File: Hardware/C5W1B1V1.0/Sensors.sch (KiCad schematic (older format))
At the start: 23 parts, among them U5 LSM303AHTR, U6 VL53L0CXV0DH_1, U7 BME688, U8 ISM330ISN

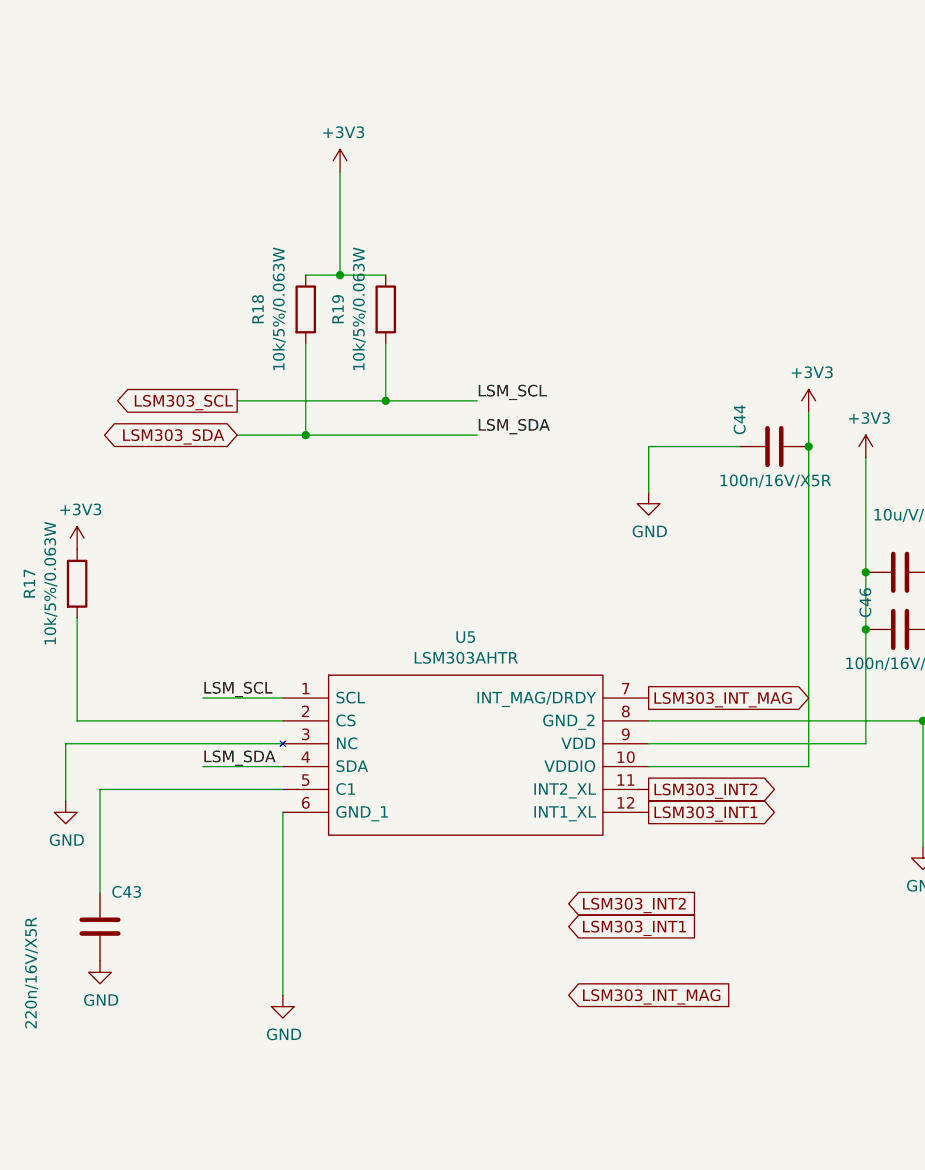
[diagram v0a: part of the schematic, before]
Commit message: Linie PC0-PE13
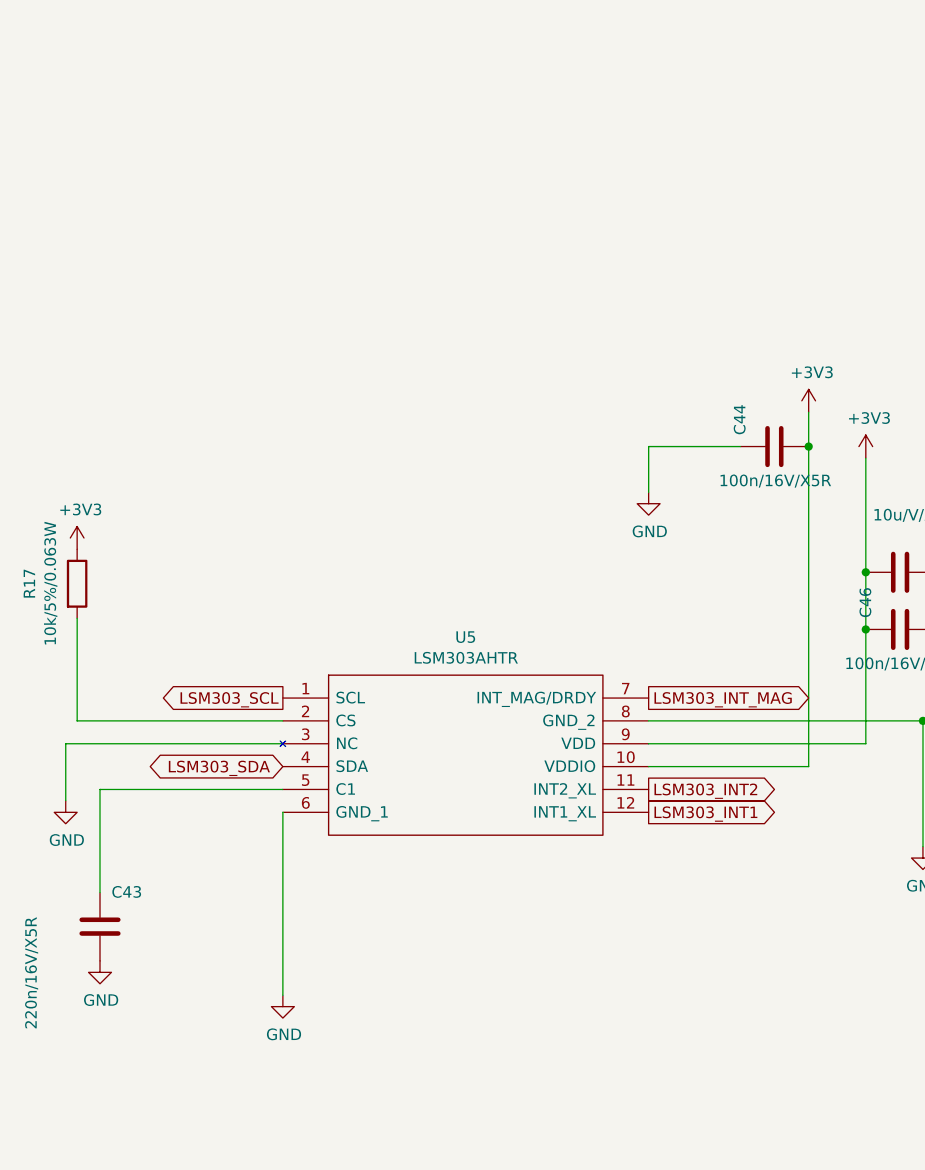
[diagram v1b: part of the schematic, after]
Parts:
- removed R18, R19: 10k/5%/0.063W, Resistor_SMD:R_0402_1005Metric, symbol Device:R
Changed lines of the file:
@@
 	1    0    0    -1
 $EndComp
-Text GLabel 3200 4400 2    50   Input ~ 0
-LSM303_INT2
-Text GLabel 3200 4500 2    50   Input ~ 0
-LSM303_INT1
-Text GLabel 3200 4800 2    50   Input ~ 0
-LSM303_INT_MAG
-Text GLabel 1750 2350 0    50   BiDi ~ 0
-LSM303_SDA
-Text GLabel 1750 2200 0    50   Output ~ 0
-LSM303_SCL
 Wire Wire Line
 	1950 3600 1050 3600
@@
 	1    0    0    -1
 $EndComp
-Text Label 1600 3500 0    50   ~ 0
-LSM_SCL
-Wire Wire Line
-	1600 3500 1950 3500
-Wire Wire Line
-	1600 3800 1950 3800
-Text Label 1600 3800 0    50   ~ 0
-LSM_SDA
-$Comp
-L Device:R R?
-U 1 1 667DEC1A
-P 2050 1800
-AR Path="/665B4F23/667DEC1A" Ref="R?"  Part="1"
-AR Path="/665B5071/667DEC1A" Ref="R18"  Part="1"
-F 0 "R18" V 1843 1800 50  0000 C CNN
-F 1 "10k/5%/0.063W" V 1934 1800 50  0000 C CNN
-F 2 "Resistor_SMD:R_0402_1005Metric" V 1980 1800 50  0001 C CNN
-F 3 "~" H 2050 1800 50  0001 C CNN
-	1    2050 1800
-	1    0    0    -1
-$EndComp
-$Comp
-L Device:R R?
-U 1 1 667E0B7A
-P 2400 1800
-AR Path="/665B4F23/667E0B7A" Ref="R?"  Part="1"
-AR Path="/665B5071/667E0B7A" Ref="R19"  Part="1"
-F 0 "R19" V 2193 1800 50  0000 C CNN
-F 1 "10k/5%/0.063W" V 2284 1800 50  0000 C CNN
-F 2 "Resistor_SMD:R_0402_1005Metric" V 2330 1800 50  0001 C CNN
-F 3 "~" H 2400 1800 50  0001 C CNN
-	1    2400 1800
-	1    0    0    -1
-$EndComp
-Wire Wire Line
-	1750 2200 2400 2200
-Wire Wire Line
-	1750 2350 2050 2350
-Wire Wire Line
-	2050 1950 2050 2350
-Connection ~ 2050 2350
-Wire Wire Line
-	2050 2350 2800 2350
-Wire Wire Line
-	2400 1950 2400 2200
-Connection ~ 2400 2200
-Wire Wire Line
-	2400 2200 2800 2200
-Wire Wire Line
-	2050 1650 2200 1650
-Wire Wire Line
-	2200 1650 2200 1200
-Connection ~ 2200 1650
-Wire Wire Line
-	2200 1650 2400 1650
-$Comp
-L power:+3V3 #PWR0239
-U 1 1 667F099D
-P 2200 1200
-F 0 "#PWR0239" H 2200 1050 50  0001 C CNN
-F 1 "+3V3" H 2215 1373 50  0000 C CNN
-F 2 "" H 2200 1200 50  0001 C CNN
-F 3 "" H 2200 1200 50  0001 C CNN
-	1    2200 1200
-	1    0    0    -1
-$EndComp
-Text Label 2800 2200 0    50   ~ 0
-LSM_SCL
-Text Label 2800 2350 0    50   ~ 0
-LSM_SDA
 Wire Wire Line
 	15650 3050 15950 3050
@@
 Text GLabel 18050 1750 2    50   Input ~ 0
 BME688_SCL
+Text GLabel 1950 3500 0    50   Output ~ 0
+LSM303_SCL
+Text GLabel 1950 3800 0    50   BiDi ~ 0
+LSM303_SDA
 $EndSCHEMATC
